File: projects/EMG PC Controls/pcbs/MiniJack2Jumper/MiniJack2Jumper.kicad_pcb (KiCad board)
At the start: 2 copper layers, 1 part, among them J1 35RASMT2BHNTRX

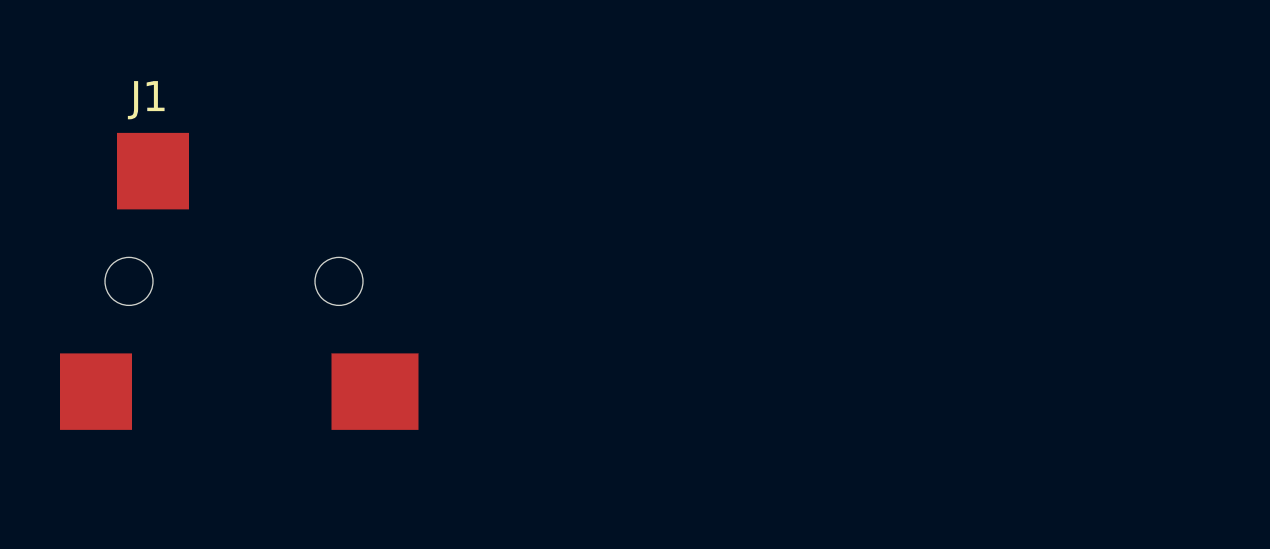
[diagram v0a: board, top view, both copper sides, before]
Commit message: added header + BOM
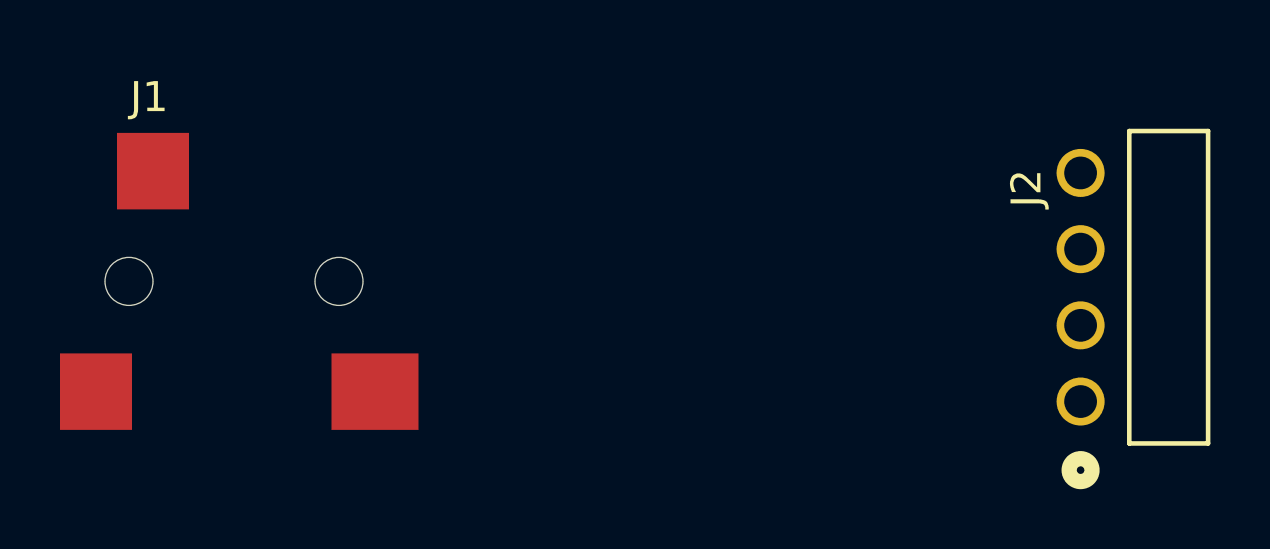
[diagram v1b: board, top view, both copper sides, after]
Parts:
- added J2: 901210124, MiniJack2Jumper:CONN04_901210124_MOL, F.Cu at (143.3, 100.0)

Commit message: finiished mini jack to 1x4 jumper pcb
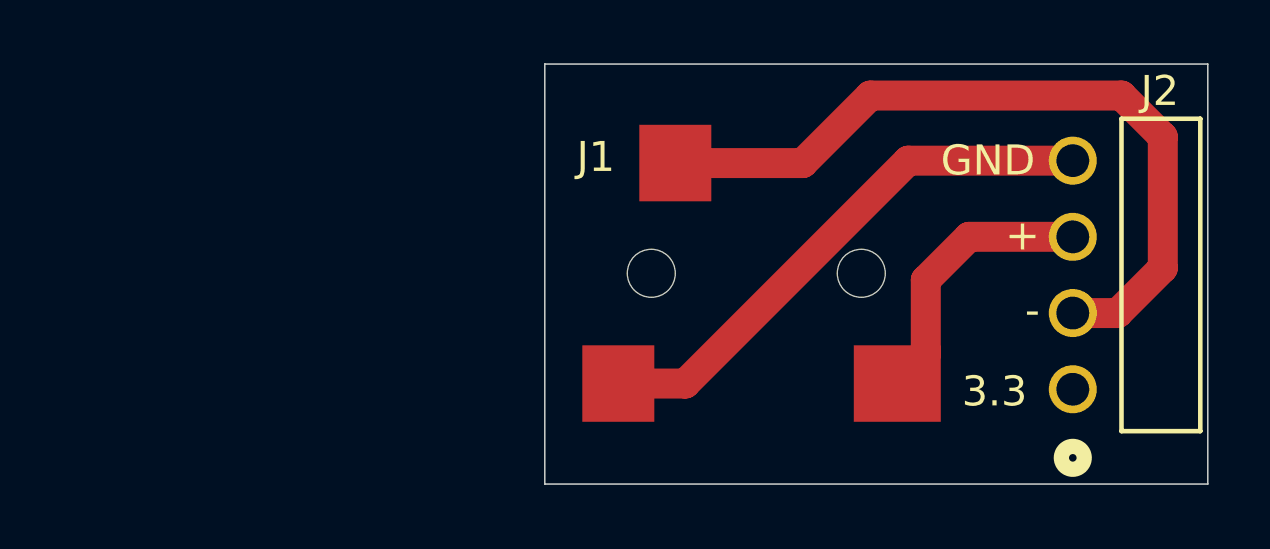
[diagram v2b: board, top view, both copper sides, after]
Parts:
- J1: value 35RASMT2BHNTRX -> SWITCHCRAFT_35RASMT2BHNTRX
- moved J1 17.4 mm to (132.4, 95.7)
- moved J2 0.49 mm to (143.0, 99.5)
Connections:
- J1 pad 1: unconnected-(J1-Pad1) -> /-IN
- J1 pad 4: unconnected-(J1-Pad4) -> /+IN
- J1 pad 5: unconnected-(J1-Pad5) -> /GND
- J2 pad 2: unconnected-(J2-Pad2) -> /-IN
- J2 pad 3: unconnected-(J2-Pad3) -> /+IN
- J2 pad 4: unconnected-(J2-Pad4) -> /GND
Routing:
- net /-IN: track 0.00 -> 25.7 mm
- net /GND: track 0.00 -> 18.2 mm
- net /+IN: track 0.00 -> 9.34 mm
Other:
- board outline added: 22.1 x 14 mm
- board text added: "+"
- board text added: "-"
- board text added: "3.3"
- board text added: "GND"
